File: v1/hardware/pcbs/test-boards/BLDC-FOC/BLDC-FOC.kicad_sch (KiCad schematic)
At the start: 16 parts, among them CN1 HB9500-3

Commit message: bldc foc test board done
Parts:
- added C39, C40: 100nF, Capacitor_SMD:C_0603_1608Metric, symbol Device:C_Small
- added C41: 4.7nF, Capacitor_SMD:C_0603_1608Metric, symbol Device:C_Small
- added J1: Conn_01x12, Connector_JST:JST_XH_S12B-XH-A_1x12_P2.50mm_Horizontal, symbol Connector_Generic:Conn_01x12
- added J2: Conn_01x10, Connector_JST:JST_XH_S10B-XH-A_1x10_P2.50mm_Horizontal, symbol Connector_Generic:Conn_01x10
- added J3: Conn_02x02_Odd_Even, Connector_PinHeader_2.54mm:PinHeader_2x02_P2.54mm_Vertical, symbol Connector_Generic:Conn_02x02_Odd_Even
- added JP1: Jumper_3_Bridged12, Connector_PinHeader_2.54mm:PinHeader_1x03_P2.54mm_Vertical, symbol Jumper:Jumper_3_Bridged12
- added R35, R36: 60, Resistor_SMD:R_0603_1608Metric, symbol Device:R_Small
- added R37, R38, R39, R40: 2.7K, Resistor_SMD:R_0603_1608Metric, symbol Device:R_Small
- added R4, R6: 32.4K, Resistor_SMD:R_0603_1608Metric, symbol Device:R_Small
- added R5, R7: 10K, Resistor_SMD:R_0603_1608Metric, symbol Device:R_Small
- added TP1, TP17, TP2, TP3, TP4, TP5, TP6, TP7: TestPoint, Connector_PinSocket_2.54mm:PinSocket_1x01_P2.54mm_Vertical, symbol Connector:TestPoint
- added U7: TXS0108EPW, Package_SO:TSSOP-20_4.4x6.5mm_P0.65mm, symbol Logic_LevelTranslator:TXS0108EPW
- added U8: TCAN1057AVDRQ1, EasyEDA:SOIC-8_L4.9-W3.9-P1.27-LS6.0-BL, symbol EasyEDA:TCAN1057AVDRQ1
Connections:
- net +3V3: now also C40.1, J1.4 (Pin_4), JP1.3 (B), R37.1, R38.1, TP17.1, U7.2 (VCCA), U8.5 (NC,VIO); no longer U1.16 (3V3)
- net +5V: now also C39.2, J1.3 (Pin_3), JP1.1 (A), R4.1, U8.3 (VCC); no longer U1.38 (PA1)
- net BOOT0: now also J1.10 (Pin_10)
- net GND: now also C39.1, C40.2, C41.1, J1.1 (Pin_1), J1.2 (Pin_2), J2.1 (Pin_1), R5.2, R7.2, TP4.1, TP7.1, U7.11 (GND), U8.2 (GND); no longer U1.37 (PA2)
- net U_HIGH_PWM: now also U1.24 (PA8)
- net U_I_SENSE: now also U1.38 (PA1)
- net U_LOW_PWM: now also U1.12 (PC13)
- net U_POWER: now also TP1.1
- net VMOT: now also TP6.1
- net VMOT_SENSE: now also U1.13 (PA0)
- net V_HIGH_PWM: now also U1.23 (PA9)
- net V_I_SENSE: now also U1.31 (PB0)
- net V_LOW_PWM: now also U1.25 (PB14)
- net V_POWER: now also TP2.1
- net W_HIGH_PWM: now also U1.3 (PA10)
- net W_I_SENSE: now also U1.32 (PA7)
- net W_LOW_PWM: now also U1.30 (PB1)
- net W_POWER: now also TP3.1
- net USART1_RX: now reaches U1.10 (PB7)
- net USART1_RX: now also U7.9 (A8)
- net NRST: now reaches U1.14 (NRST)
- net NRST: now also J1.9 (Pin_9)
- net FDCAN2_TX: now reaches U1.26 (PB13)
- net FDCAN2_TX: now also U8.1 (TXD)
- net FDCAN2_RX: now reaches U1.27 (PB12)
- net FDCAN2_RX: now also U8.4 (RXD)
- net SHIFTER_OE: now reaches U1.28 (PB11)
- net SHIFTER_OE: now also U7.10 (OE)
- net CAN_SILENT: now reaches U1.29 (PB2)
- net CAN_SILENT: now also U8.8 (S)
- net 12V_SENSE: now reaches U1.33 (PA6)
- net 12V_SENSE: now also R6.2, R7.1
- net 5V_SENSE: now reaches U1.34 (PA5)
- net 5V_SENSE: now also R4.2, R5.1
- net SPI1_SCS: now reaches U1.35 (PA4)
- net SPI1_SCS: now also U7.7 (A6)
- net USART2_RX: now reaches U1.36 (PA3)
- net USART2_RX: now also J1.7 (Pin_7)
- net I2C1_SDA: now reaches U1.4 (PB9)
- net I2C1_SDA: now also R37.2, U7.1 (A1)
- net I2C1_SCL: now reaches U1.5 (PA15)
- net I2C1_SCL: now also R38.2, U7.3 (A2)
- net SPI1_SCLK: now reaches U1.6 (PB3)
- net SPI1_SCLK: now also U7.6 (A5)
- net SPI1_MISO: now reaches U1.7 (PB4)
- net SPI1_MISO: now also U7.5 (A4)
- net SPI1_MOSI: now reaches U1.8 (PB5)
- net SPI1_MOSI: now also U7.4 (A3)
- net USART1_TX: now reaches U1.9 (PB6)
- net USART1_TX: now also U7.8 (A7)
- net SK6812_data: no longer names the net of U1.15 (SK6812_data)
- net VGATE renamed +12V
- net +12V: now also R6.1, TP5.1
- new net: J3.3 (Pin_3), R35.1
- new net: J3.1 (Pin_1), R36.2
- new net: C41.2, J3.2 (Pin_2), J3.4 (Pin_4)
- new net CAN+: J1.11 (Pin_11), J1.6 (Pin_6), R36.1, U8.7 (CANH)
- new net CAN-: J1.12 (Pin_12), J1.5 (Pin_5), R35.2, U8.6 (CANL)
- new net ENC_VCC: J2.2 (Pin_2), JP1.2 (C), R39.1, R40.1, U7.19 (VCCB)
- new net I2C1_SCL_ENC: J2.9 (Pin_9), R40.2, U7.18 (B2)
- new net I2C1_SDA_ENC: J2.10 (Pin_10), R39.2, U7.20 (B1)
- new net SPI1_MISO_ENC: J2.7 (Pin_7), U7.16 (B4)
- new net SPI1_MOSI_ENC: J2.8 (Pin_8), U7.17 (B3)
- new net SPI1_SCLK_ENC: J2.6 (Pin_6), U7.15 (B5)
- new net SPI1_SCS_ENC: J2.5 (Pin_5), U7.14 (B6)
- new net USART1_RX_ENC: J2.3 (Pin_3), U7.12 (B8)
- new net USART1_TX_ENC: J2.4 (Pin_4), U7.13 (B7)
- new net USART2_TX: J1.8 (Pin_8), U1.37 (PA2)
- no-connect marks 0 -> 5
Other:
- removed sheet LM5164
- added sheet power (power.kicad_sch)
- note added: "I/O"
- note added: "POWER & PROTECTION"
- note added: "TIMERS: TIM1_CH1: PA8 (U_HIGH_PWM) TIM1_CH1N: PC13 (U_LOW_PWM) TIM1_CH2: PA9 (V_HIGH_PWM) TIM1_CH2N: PB14 (V_LOW_PWM) TIM1_CH3: PA10 (W_HIGH_PWM) TIM1_CH3N: PB1 (W_LOW_PWM) OPAMPS (PGA internally connected, noninverting): OPAMP1_VINP: PA7 (W_I_SENSE) OPAMP2_VINP: PB0 (V_I_SENSE) OPAMP3_VINP: PA1 (U_I_SENSE) ADCS: ADC1_IN1: PA0 (VMOT_SENSE) ADC2_IN3: PA6 (12V_SENSE) ADC2_IN13: PA5 (5V_SENSE) I/O: 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"
- note added: "VOLTAGE_SENSE"
- note added: "install jumpers across: 1&2 3&4 for termination"
- note removed: "GATE BUCK"
- note removed: "this is around 16V"
- moved on the sheet: C1, C10, C11, C2, C3, C4, C9, CN1, D1, D2, D3, GDRV1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

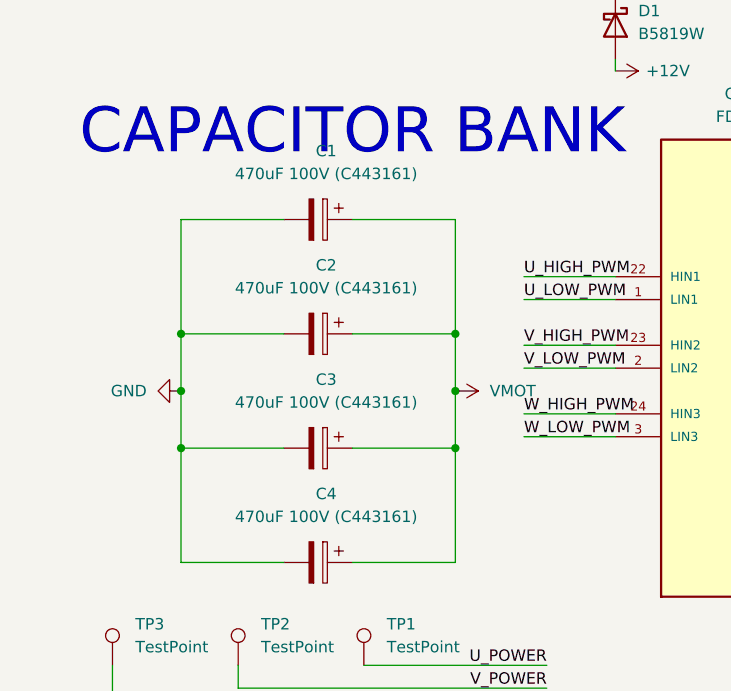
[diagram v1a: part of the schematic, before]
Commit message: updated capacitors to be larger ones
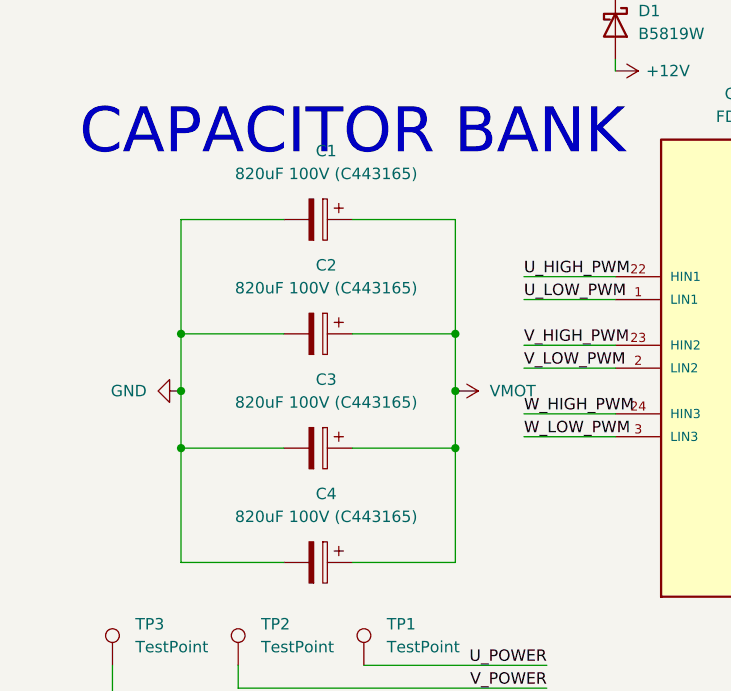
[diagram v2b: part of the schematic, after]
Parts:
- C1, C2, C3, C4: value 470uF 100V (C443161) -> 820uF 100V (C443165)
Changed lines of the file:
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@@
 			)
 		)
-		(property "Value" "470uF 100V (C443161)"
+		(property "Value" "820uF 100V (C443165)"
 			(at 41.529 113.03 90)
 			(effects
@@
 			)
 		)
-		(property "Value" "470uF 100V (C443161)"
+		(property "Value" "820uF 100V (C443165)"
 			(at 41.529 125.73 90)
 			(effects
@@
 			)
 		)
-		(property "Value" "470uF 100V (C443161)"
+		(property "Value" "820uF 100V (C443165)"
 			(at 41.529 87.63 90)
 			(effects
@@
 			)
 		)
-		(property "Value" "470uF 100V (C443161)"
+		(property "Value" "820uF 100V (C443165)"
 			(at 41.529 100.33 90)
 			(effects

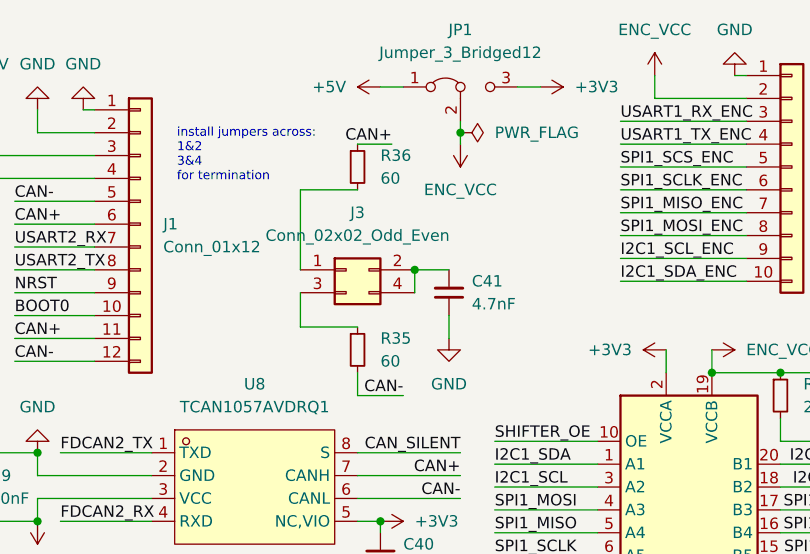
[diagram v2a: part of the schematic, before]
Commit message: larger resistors for high voltages, new prod files
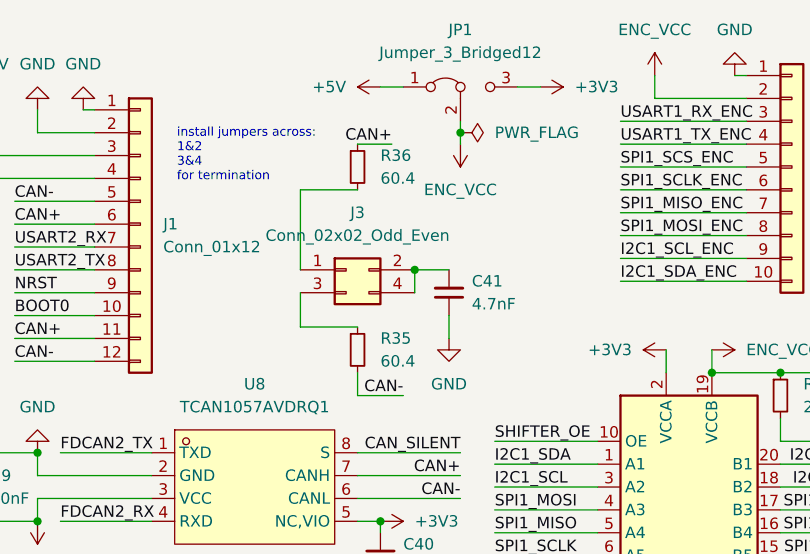
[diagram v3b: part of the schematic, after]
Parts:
- R1: footprint Resistor_SMD:R_0603_1608Metric -> Resistor_SMD:R_0805_2012Metric
- R35, R36: value 60 -> 60.4
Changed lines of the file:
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@@
 			)
 		)
-		(property "Value" "60"
+		(property "Value" "60.4"
 			(at 223.52 52.07 0)
 			(effects
@@
 			)
 		)
-		(property "Value" "60"
+		(property "Value" "60.4"
 			(at 223.52 31.75 0)
 			(effects
@@
 			)
 		)
-		(property "Footprint" "Resistor_SMD:R_0603_1608Metric"
+		(property "Footprint" "Resistor_SMD:R_0805_2012Metric"
 			(at 135.89 93.98 0)
 			(effects

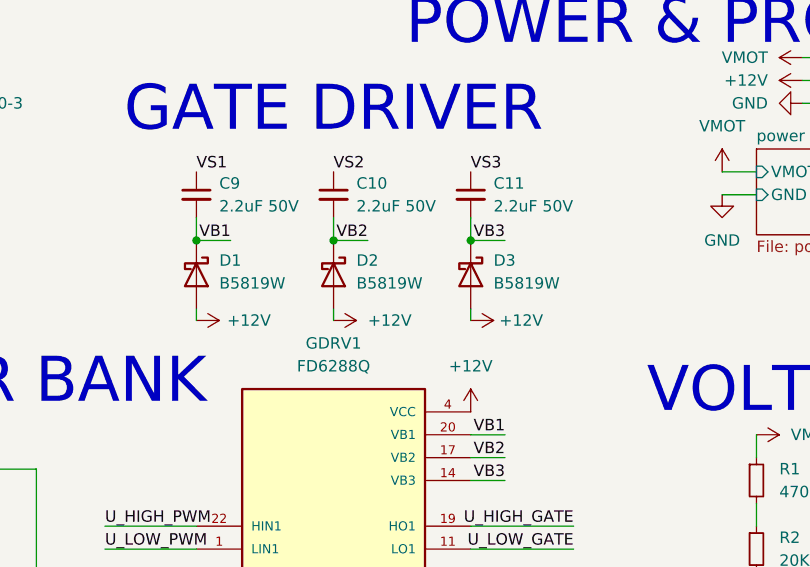
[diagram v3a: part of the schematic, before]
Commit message: fixed bootstrap diodes to have proper voltage ratings
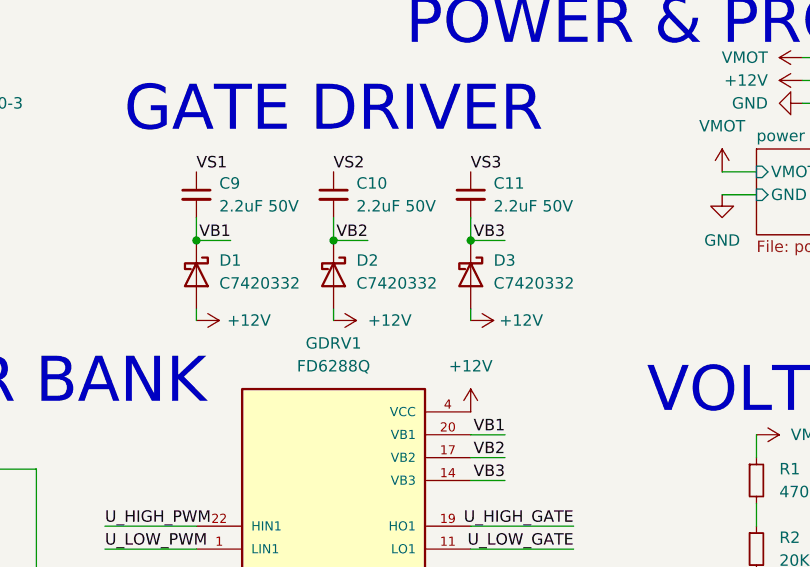
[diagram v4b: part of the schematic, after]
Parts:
- D1, D2, D3: value B5819W -> C7420332
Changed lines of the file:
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@@
 			)
 		)
-		(property "Value" "B5819W"
+		(property "Value" "C7420332"
 			(at 91.44 72.0725 90)
 			(effects
@@
 			)
 		)
-		(property "Value" "B5819W"
+		(property "Value" "C7420332"
 			(at 106.68 72.0725 90)
 			(effects
@@
 			)
 		)
-		(property "Value" "B5819W"
+		(property "Value" "C7420332"
 			(at 76.2 72.0725 90)
 			(effects
